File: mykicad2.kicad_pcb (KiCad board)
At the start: 2 copper layers, 9 parts, among them P1 CONN_01X06, Q1 MMBT3904, Q2 MMBT3906

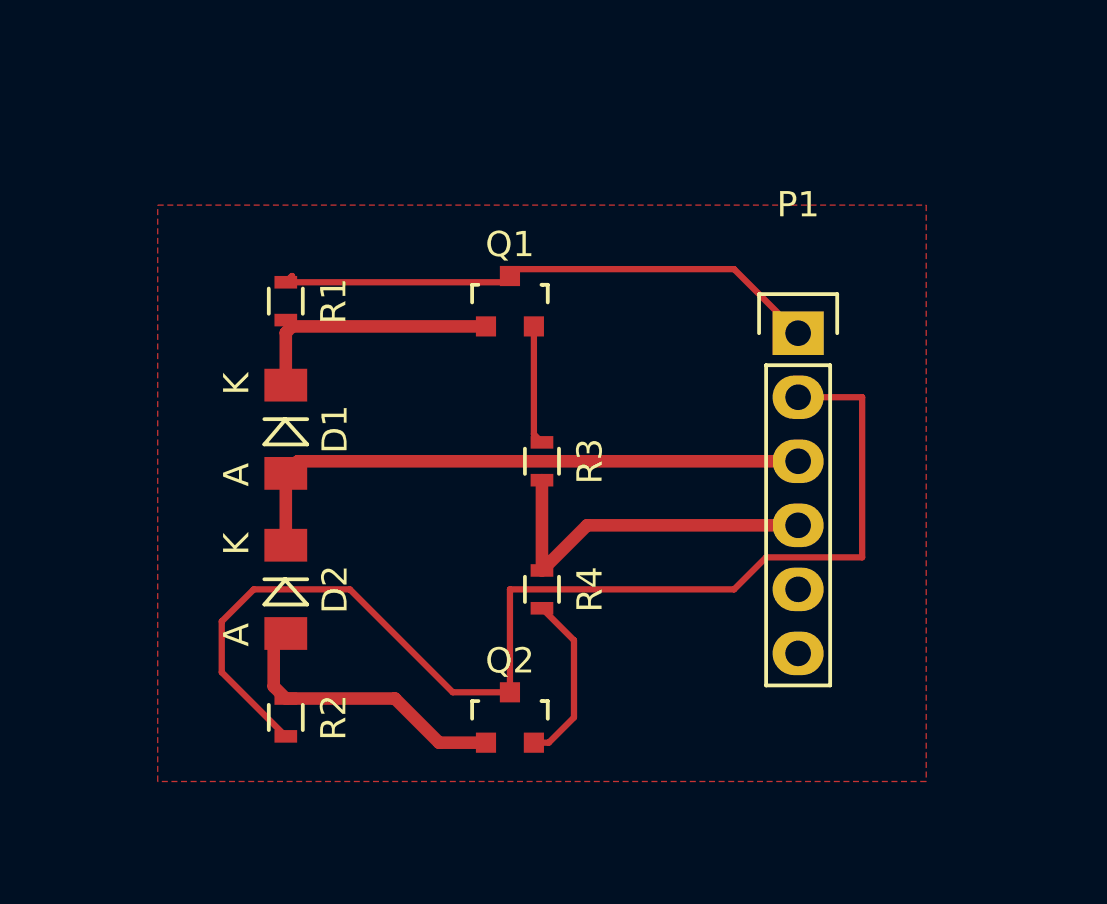
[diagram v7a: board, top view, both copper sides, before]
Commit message: relayout with mosfet
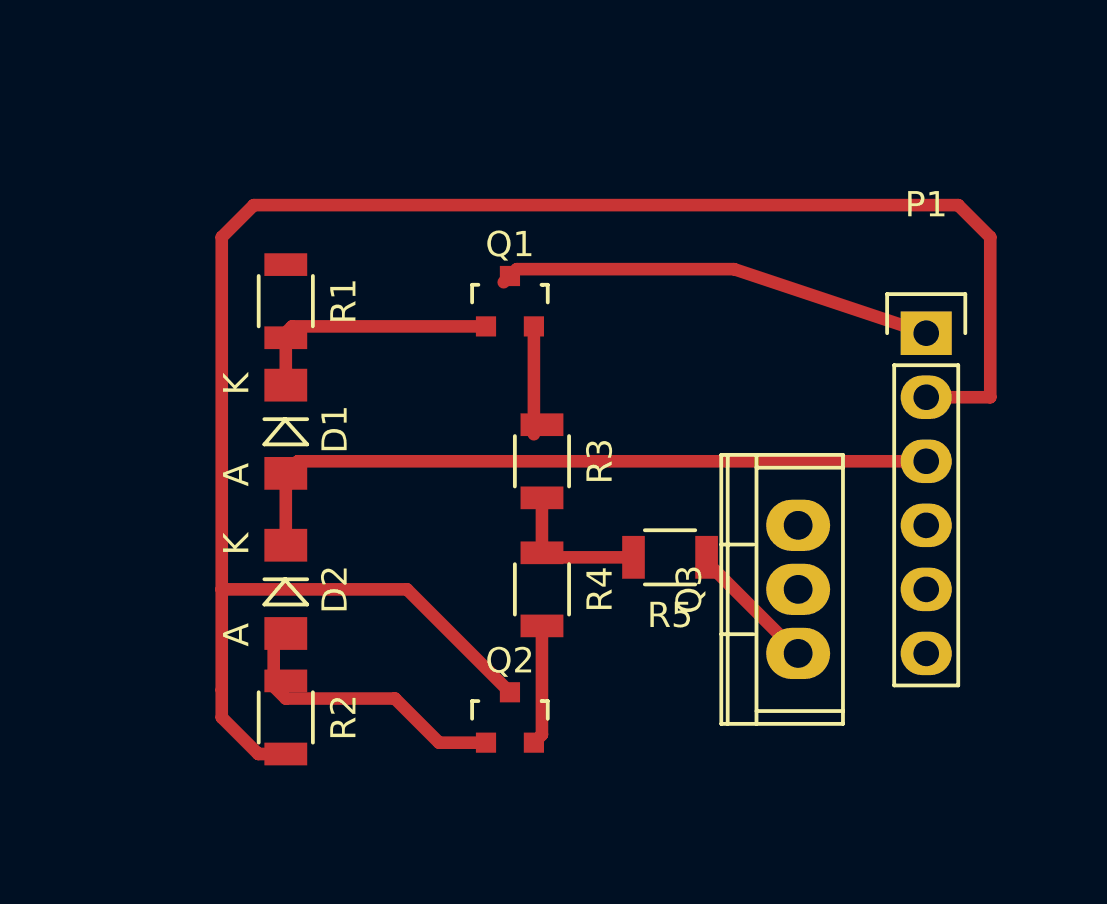
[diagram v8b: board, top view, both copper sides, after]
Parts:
- added Q3: IRF9540N, Power_Integrations:TO-220, F.Cu at (170.2, 108.0)
- added R5: R, Resistors_SMD:R_1206, F.Cu at (165.1, 106.7)
- R1, R2, R3, R4: footprint Resistors_SMD:R_0603 -> Resistors_SMD:R_1206
- moved P1 5.08 mm to (175.3, 97.8)
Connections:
- R3 pad 2: Net-(P1-Pad4) -> Net-(R3-Pad2)
- R4 pad 1: Net-(P1-Pad4) -> Net-(R3-Pad2)
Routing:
- net GND: track 46.7 -> 75.7 mm
- net Net-(P1-Pad4): track 14.5 -> 0.00 mm
- net Net-(R3-Pad2): track 0.00 -> 5.88 mm
- net Net-(Q3-Pad1): track 0.00 -> 5.31 mm
- net Net-(D1-Pad2): track 23.4 -> 28.4 mm
- net VDD: track 22.3 -> 17.4 mm
- net Net-(Q2-Pad2): track 6.86 -> 4.76 mm
- removed copper zone on F.Cu, net GND
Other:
- net class Default: trace_width 0.25 -> 0.5; via_dia 0.6 -> 0.7
